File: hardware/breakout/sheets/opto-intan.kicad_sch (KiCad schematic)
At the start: 36 parts, among them J46 Intan opto out: EVT_STROBE_IN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, J47 Intan opto out: BARCODE_INTAN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, J48 Intan opto out: RWD_CMD_INTAN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, J49 Intan opto out: RWD_DLVR_INTA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, J50 Intan opto out: STIM_TRIG_INT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, J51 Intan RHS stim status in (BNC), U63 TMR 1-0511, U64 ACSL-6400-00TE, U65 ACSL-6420-00TE

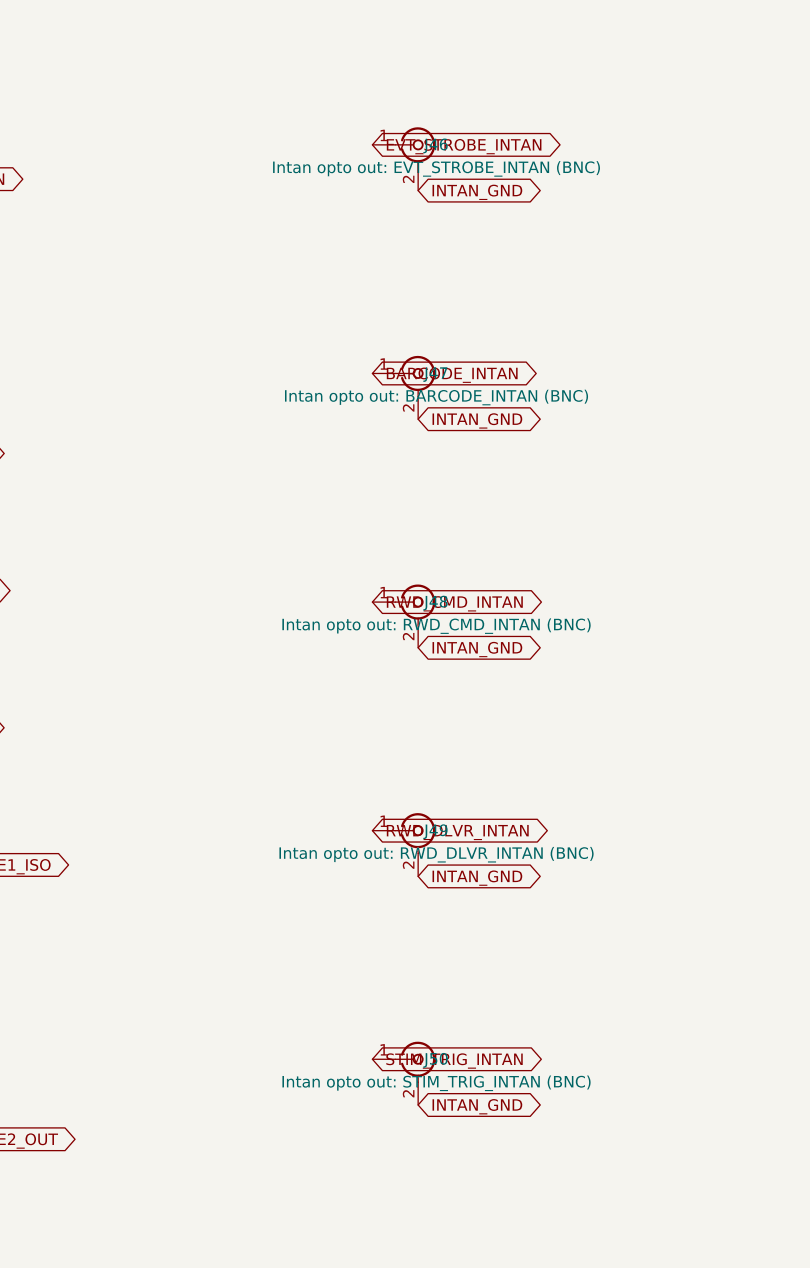
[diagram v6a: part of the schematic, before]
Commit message: fix(hardware): one driver and one series resistor per panel output (F4, M3)
F4 -- FOUR CAMERA TRIGGERS SHARED ONE UNTERMINATED OUTPUT.

CAM_TRIG_BEH drove J14-J17 from a single SN74AHCT541 output. Four parallel
coax runs present Z0/4 ~ 12.5 ohm, so the initial edge drew roughly 118 mA
against the part's 25 mA per-output ABSOLUTE maximum -- brief, but on every
edge for the life of the board. With no source termination the cameras
could also see reflections and double-trigger, which is corrupted frame
timing rather than a cosmetic fault.

Each of the five triggers now has its own buffer channel and its own 47 ohm
series resistor: CAM_TRIG_BEH splits into CAM_TRIG_BEH1..4, channel 2 of the
existing trigger buffer keeps trigger 1, and a new package (U74) takes the
other three. They still share one trigger RATE via CAM_TRIG_BEH_RAW -- spec
Sec.9.4 is unchanged -- they no longer share a driver pin.

NOT on finding F1's spare channels, which the audit expected. Those sit on
taskpc-digital, and routing an unbuffered 3.3 V trigger across the board and
its buffered copies back again is the wrong trade for a signal whose entire
problem is edge quality at the connector. Source GPIO, buffer and BNCs stay
on one sheet; the cost is one package.

47 ohm errs high on purpose. An AHCT541's own output impedance is ~25-35
ohm, so textbook series termination into 50 ohm coax would be nearer 20 ohm.
Over-damping costs a little edge rate and buys margin against the failure
that actually matters here. The first step at a high-impedance camera input
lands at ~77% of the swing before settling, far above any TTL V_IH.

M3 -- SIX BARE PANEL OUTPUTS, AND THERE WERE ELEVEN.

Series resistance added to all six the finding names: the five camera
triggers at 47 ohm, and J6 (reward driver out) at 100 ohm -- that pin's
problem is fault current from an inductive kick or a mis-plug, not
transmission-line matching, so it takes this board's established
panel-series value rather than the termination one. 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
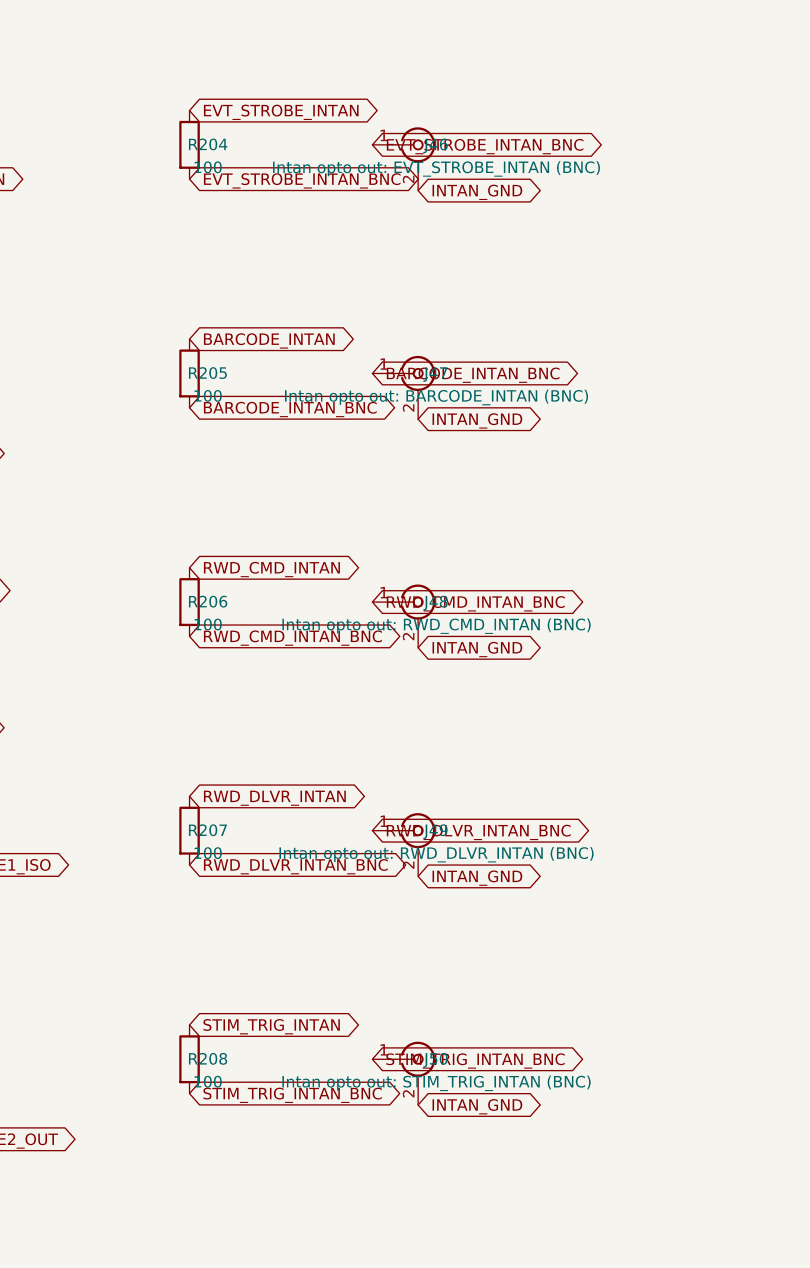
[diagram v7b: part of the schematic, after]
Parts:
- added R204, R205, R206, R207, R208: 100, Resistor_SMD:R_0603_1608Metric, symbol Device:R
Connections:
- net BARCODE_INTAN: now also R205.1; no longer J47.1 (In)
- net EVT_STROBE_INTAN: now also R204.1; no longer J46.1 (In)
- net RWD_CMD_INTAN: now also R206.1; no longer J48.1 (In)
- net RWD_DLVR_INTAN: now also R207.1; no longer J49.1 (In)
- net STIM_TRIG_INTAN: now also R208.1; no longer J50.1 (In)
- new net BARCODE_INTAN_BNC: J47.1 (In), R205.2
- new net EVT_STROBE_INTAN_BNC: J46.1 (In), R204.2
- new net RWD_CMD_INTAN_BNC: J48.1 (In), R206.2
- new net RWD_DLVR_INTAN_BNC: J49.1 (In), R207.2
- new net STIM_TRIG_INTAN_BNC: J50.1 (In), R208.2

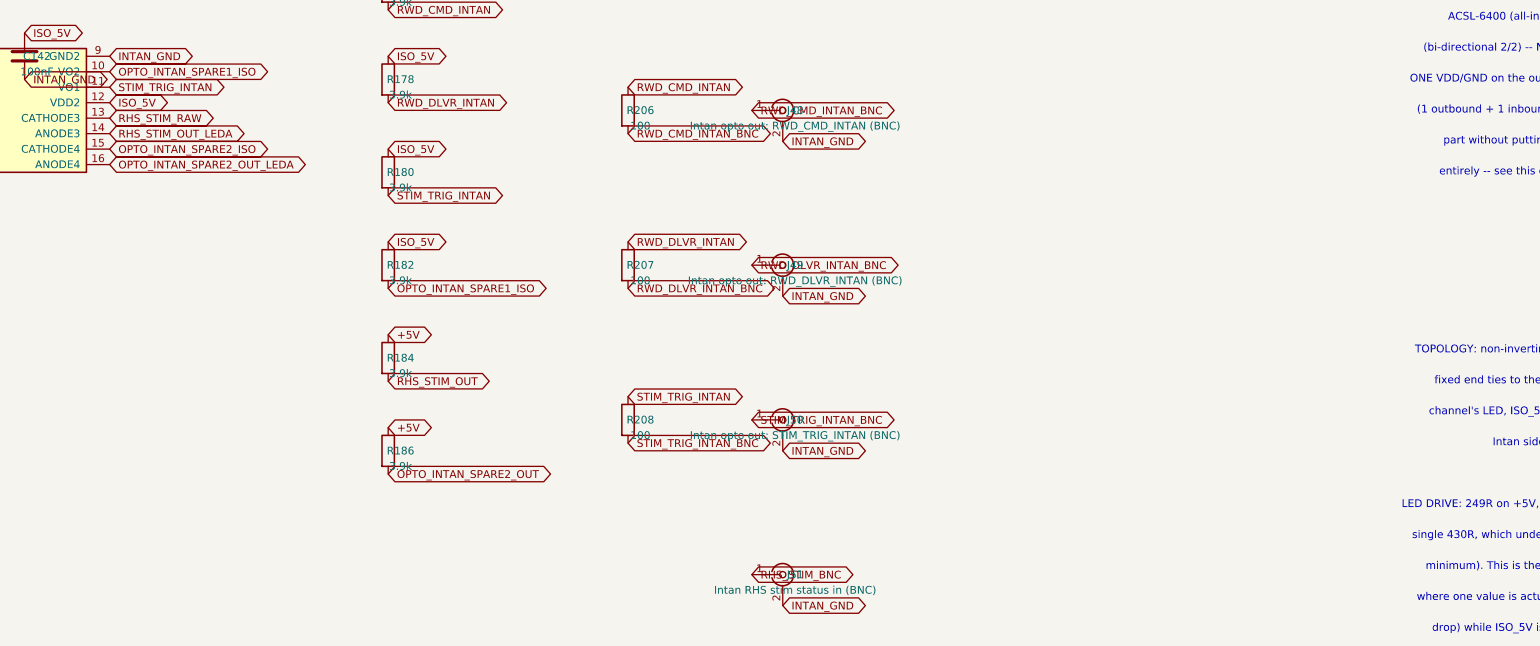
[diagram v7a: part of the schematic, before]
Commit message: fix(hardware): buffer the inbound stim channel locally (F2)
Two defects in one wire, and the checker that should have caught the first
was itself wrong about it.

THE 100R PANEL RESISTOR WAS INSIDE THE LED'S CURRENT LOOP.
ISO_5V -> 301R -> LED -> 100R -> Intan's output, so the loop was 401R and
the branch delivered 6.57 mA worst case against the ACSL-6xx0's 7.0 mA
I_FH minimum. Not guaranteed to switch. This was the only channel on the
board whose protection resistor did double duty as a current-setting one.

IT ALSO DEPENDED ON A PHYSICAL SWITCH NOBODY DOCUMENTED. The Intan
Stim/Recording Controller's CONFIG4 selects whether its digital outputs are
3.3 V or 5.0 V. With CONFIG4 DOWN the LED anode sits at ISO_5V while its
cathode rests at 3.3 V, leaking roughly 1.3 mA against a 250 uA I_FL limit
-- the channel may never turn cleanly OFF. The as-built design was correct
for one undocumented switch position and silently wrong for the other.

A local SN74AHCT541PW (U75) on ISO_5V, referenced INTAN_GND, now drives the
LED: RHS_STIM_BNC -> 100R -> RHS_STIM_RAW (clamped) -> buffer ->
RHS_STIM_ISO_BUF -> LED cathode. The 100R and the BAT54S do protection
ONLY. The branch is 301R and 8.75-12.92 mA, identical to the spare channel
beside it.

THE CONFIG4 DEPENDENCY IS RETIRED, NOT MERELY RECORDED. Both the finding
and the handoff said to note "CONFIG4 UP" as something no checker can see.
That turned out to be unnecessary: an AHCT part's TTL thresholds (V_IH
2.0 V) are independent of its own supply, so the buffer reads a 3.3 V or a
5.0 V input as a valid HIGH either way, and its rail-to-rail output gives
the LED a clean 0 V off-state. CONFIG4 UP is still worth setting and is
recorded in hardware/README.md beside RewardPolarity HIGH, but as a rig
preference rather than a correctness dependency. Worth remembering when a
finding says "record this and move on" -- sometimes the fix already being
made removes the need.

A GAP IN THIS REPO'S OWN CHECKER, FIXED FIRST.
Check 15 (finding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
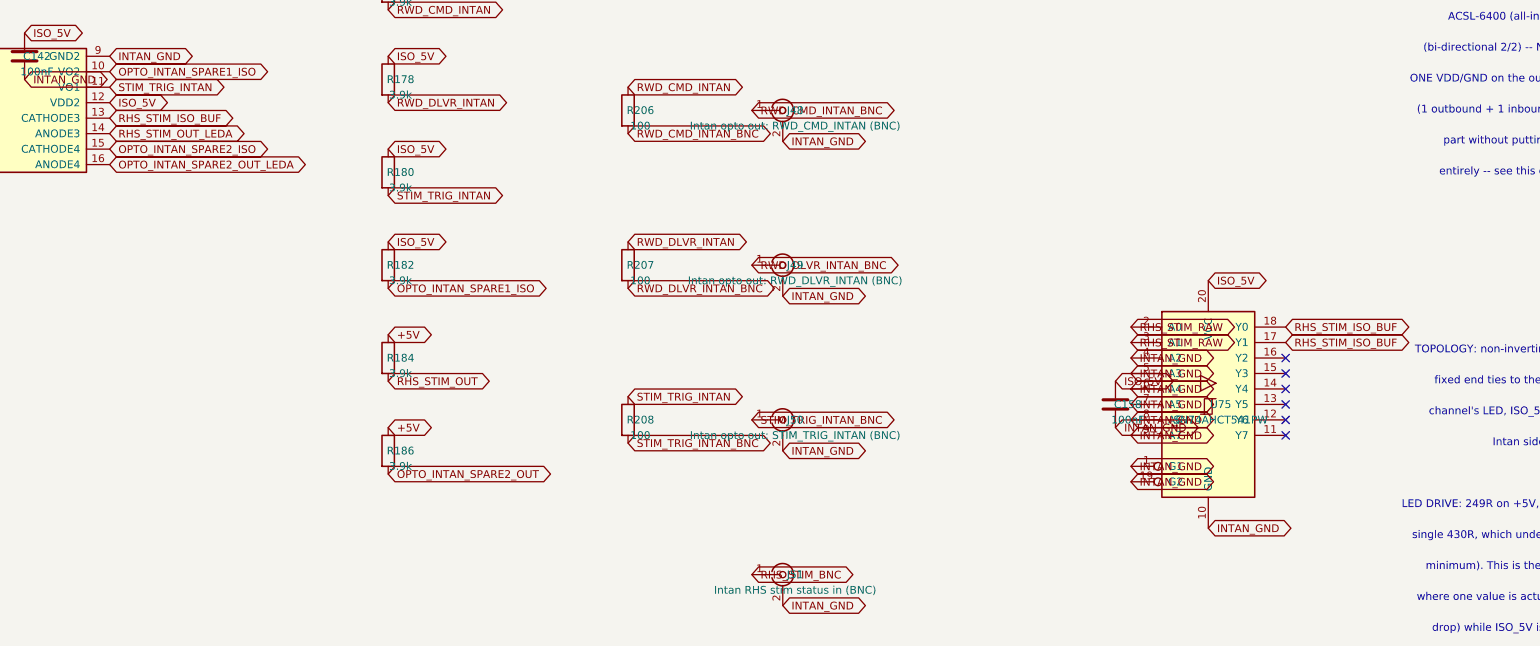
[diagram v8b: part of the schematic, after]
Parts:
- added C158: 100nF, Capacitor_SMD:C_0603_1608Metric, symbol Device:C
- added U75: SN74AHCT541PW, Package_SO:Texas_PW0020A_TSSOP-20_4.4x6.5mm_P0.65mm, symbol 74xx:74AHCT541
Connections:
- net INTAN_GND: now also C158.2, U75.1 (G1), U75.10 (GND), U75.19 (G2), U75.4 (A2), U75.5 (A3), U75.6 (A4), U75.7 (A5), U75.8 (A6), U75.9 (A7)
- net ISO_5V: now also C158.1, U75.20 (VCC)
- net RHS_STIM_RAW: now also U75.2 (A0), U75.3 (A1); no longer U65.13 (CATHODE3)
- new net RHS_STIM_ISO_BUF: U65.13 (CATHODE3), U75.17 (Y1), U75.18 (Y0)
- no-connect marks 0 -> 6
